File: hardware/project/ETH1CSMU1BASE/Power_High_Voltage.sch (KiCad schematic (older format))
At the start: 124 parts

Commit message: Power supply design
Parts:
- removed C?: 1u/50V, symbol Device:C
- removed C? (x3): 4p7, symbol Device:C
- removed C? (x7): 1u, symbol Device:C
- removed C?: 220n, Capacitor_SMD:C_0603_1608Metric_Pad1.05x0.95mm_HandSolder, symbol Device:C
- removed C? (x2): 10u/100V, symbol Device:C
- removed C? (x3): 1u/250V, symbol Device:C
- removed C?: 100n, symbol Device:C
- removed C? (x6): 4u7/50V, symbol Device:C
- removed C? (x4): 2u2/50V, symbol Device:C
- removed D? (x3): RGF1G-E3/67A, symbol Device:D
- removed D? (x2): PMEG6010CEJ, symbol Device:D
- removed FB? (x2): Ferrite_Bead, symbol Device:Ferrite_Bead
- removed FB? (x2): 742792040, symbol Device:Ferrite_Bead
- removed L?: 330u, symbol Device:L
- removed L?: 100u, symbol Device:L
- removed L? (x4): 74489440068, symbol ETH1CSMU1:74489440068
- removed R? (x8): 1M, symbol Device:R
- removed R?: 215k, symbol Device:R
- removed R?: 10, symbol Device:R
- removed R? (x4): R, symbol Device:R
- removed R? (x2): 154k, symbol Device:R
- removed R? (x3): 287k, symbol Device:R
- removed U? (x2): LT8331EMSE#PBF, ETH1CSMU1:MSE-16, symbol ETH1CSMU1:LT8331
- removed U? (x2): LT8330_S6, symbol ETH1CSMU1:LT8330_S6
- removed U?: MC7815ABD2TR4G, symbol Regulator_Linear:L7815
- removed U?: MC7915BD2TG, symbol Regulator_Linear:L7915
- added C804, C837, C838, C864: 10u/50V, symbol Device:C
- added C805: 4u7/100V, symbol Device:C
- added C808, C824, C828, C832, C844, C861, C862, C863: 4u7/50V, symbol Device:C
- added C809, C815, C848, C851: 1u, symbol Device:C
- added C810: 10n, symbol Device:C
- added C816, C845, C855: 1u/HC, symbol Device:C
- added C819, C820, C852, C860: 4p7, symbol Device:C
- added C821, C825, C856, C858: 1u/400V, symbol Device:C
- added C829: 10u/100V, symbol Device:C
- added C841: 220n, symbol Device:C
- added D801: RB558VA150TR, symbol Device:D_Schottky
- added D802, D807: PMEG6010EP,115, symbol Device:D_Schottky
- added D803, D806: BAV21W, symbol Device:D_Schottky
- added L706, L709, L713, L716: 74489440068, symbol ETH1CSMU1:74489440068
- added L803: 744066101, symbol Device:L
- added L804: CDRH8D43RT125NP-331, symbol Device:L
- added R801, R803, R806, R808, R810, R823, R826, R828: 1M, symbol Device:R
- added R802, R821: 215k, symbol Device:R
- added R804, R824: 287k, symbol Device:R
- added R805: 63k4, symbol Device:R
- added R807: 13k3, symbol Device:R
- added R809: 97k6, symbol Device:R
- added R822: 154k, symbol Device:R
- added R825: 10/2W, symbol Device:R
- added R827: 6k7, symbol Device:R
- added R829: 46k4, symbol Device:R
- added U801, U808: LT8331, symbol ETH1CSMU1:LT8331
- added U802, U809: LT8330_S6, symbol ETH1CSMU1:LT8330_S6
- added U805: MC7815BD2TG, symbol Regulator_Linear:L7815
- added U810: MC7915BD2TG, Package_TO_SOT_SMD:TO-252-2, symbol Regulator_Linear:MC79M15_TO252
- C843, C847, C854, C859: renamed from C?; value 100n/100V -> 100n/200V
- C850: renamed from C?; value 10u/50V -> 10u/200V
- gave numbers to parts that had none: 51
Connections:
- net labels added: GNDF, GNDO
- net labels removed: GNDHV
- wire segments 448 -> 454
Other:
- note removed: "744066100"
- note removed: "CDRH8D43RT125NP‐331MC"
- moved on the sheet: C802, C803, C806, C807, C811, C812, C813, C814, C817, C818, C822, C823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

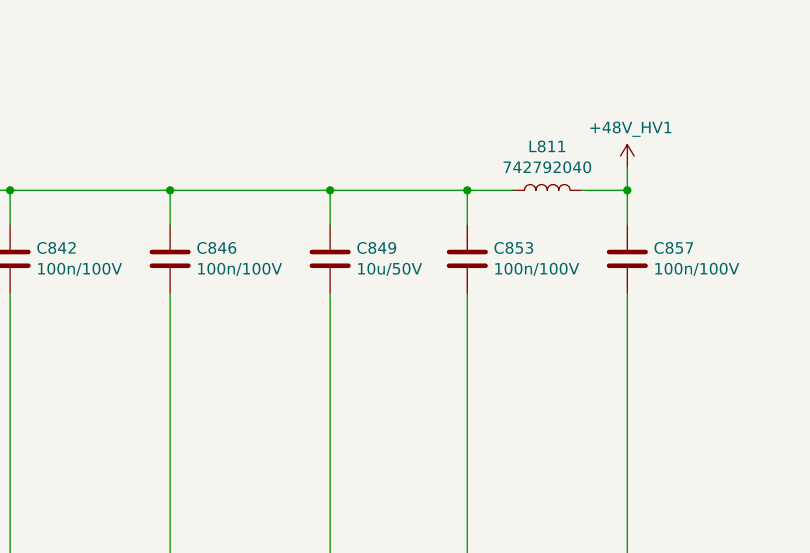
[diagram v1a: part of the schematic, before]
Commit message: Footprint assigment
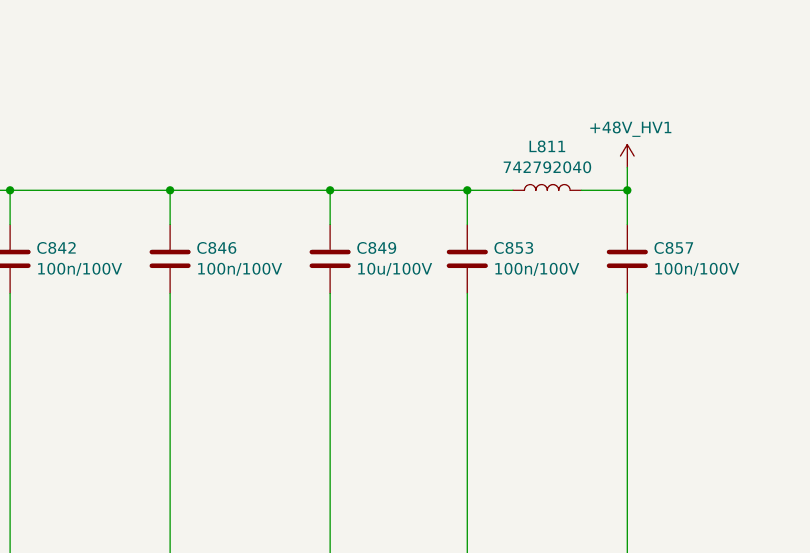
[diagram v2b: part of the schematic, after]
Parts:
- C802, C803, C804, C806, C807, C808, C817, C818, C824, C826, C827, C828, C832, C837, C838, C844, C861, C862, C863, C864: footprint (none) -> Capacitor_SMD:C_1206_3216Metric_Pad1.42x1.75mm_HandSolder
- C809, C810, C815, C819, C820, C830, C831, C833, C834, C835, C836, C839, C840, C841, C848, C851, C852, C860: footprint (none) -> Capacitor_SMD:C_0603_1608Metric_Pad1.05x0.95mm_HandSolder
- C829: footprint (none) -> Capacitor_SMD:C_2220_5650Metric_Pad1.97x5.40mm_HandSolder
- C849: value 10u/50V -> 10u/100V; footprint (none) -> Capacitor_SMD:C_1206_3216Metric_Pad1.42x1.75mm_HandSolder
- D802, D807: footprint (none) -> Diode_SMD:D_SOD-128
- D803, D806: footprint (none) -> Diode_SMD:D_SOD-123F
- L706, L709, L713, L716: footprint (none) -> ETH1CSMU1:74489440068
- R801, R802, R803, R804, R805, R808, R809, R810, R811, R812, R813, R814, R815, R816, R817, R818, R819, R820, R821, R822, R823, R824, R828, R829: footprint (none) -> Resistor_SMD:R_0603_1608Metric_Pad1.05x0.95mm_HandSolder
- U801, U806, U807, U808: footprint (none) -> Package_SO:MSOP-12-16-1EP_3x4mm_P0.5mm_EP1.65x2.85mm
- U802, U809: footprint (none) -> Package_TO_SOT_SMD:TSOT-23-6_HandSoldering
- U805: footprint (none) -> Package_TO_SOT_SMD:TO-263-2
- U810: footprint Package_TO_SOT_SMD:TO-252-2 -> Package_TO_SOT_SMD:TO-263-2

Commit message: Footprint assignment
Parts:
- C604: renamed from C805; footprint (none) -> Capacitor_SMD:C_1210_3225Metric_Pad1.42x2.65mm_HandSolder
- C610: renamed from C811; footprint (none) -> Capacitor_SMD:C_1210_3225Metric_Pad1.42x2.65mm_HandSolder
- C611: renamed from C812; footprint (none) -> Capacitor_SMD:C_1210_3225Metric_Pad1.42x2.65mm_HandSolder
- C612: renamed from C813; footprint (none) -> Capacitor_SMD:C_1210_3225Metric_Pad1.42x2.65mm_HandSolder
- C613: renamed from C814; footprint (none) -> Capacitor_SMD:C_1210_3225Metric_Pad1.42x2.65mm_HandSolder
- C615: renamed from C816; footprint (none) -> Capacitor_SMD:C_1206_3216Metric_Pad1.42x1.75mm_HandSolder
- C618: renamed from C822; footprint (none) -> Capacitor_SMD:C_2220_5650Metric_Pad1.97x5.40mm_HandSolder
- C619: renamed from C823; footprint (none) -> Capacitor_SMD:C_2220_5650Metric_Pad1.97x5.40mm_HandSolder
- C624: renamed from C821; footprint (none) -> Capacitor_SMD:C_2220_5650Metric_Pad1.97x5.40mm_HandSolder
- C626: renamed from C825; footprint (none) -> Capacitor_SMD:C_2220_5650Metric_Pad1.97x5.40mm_HandSolder
- C642: renamed from C845; footprint (none) -> Capacitor_SMD:C_1206_3216Metric_Pad1.42x1.75mm_HandSolder
- C644: renamed from C842; footprint (none) -> Capacitor_SMD:C_1206_3216Metric_Pad1.42x1.75mm_HandSolder
- C645: renamed from C843; value 100n/200V -> 100n/100V; footprint (none) -> Capacitor_SMD:C_1206_3216Metric_Pad1.42x1.75mm_HandSolder
- C646: renamed from C846; footprint (none) -> Capacitor_SMD:C_1206_3216Metric_Pad1.42x1.75mm_HandSolder
- C647: renamed from C847; value 100n/200V -> 100n/100V; footprint (none) -> Capacitor_SMD:C_1206_3216Metric_Pad1.42x1.75mm_HandSolder
- C649: renamed from C849; footprint Capacitor_SMD:C_1206_3216Metric_Pad1.42x1.75mm_HandSolder -> Capacitor_SMD:C_2220_5650Metric_Pad1.97x5.40mm_HandSolder
- C650: renamed from C850; value 10u/200V -> 10u/100V; footprint (none) -> Capacitor_SMD:C_2220_5650Metric_Pad1.97x5.40mm_HandSolder
- C652: renamed from C855; footprint (none) -> Capacitor_SMD:C_1206_3216Metric_Pad1.42x1.75mm_HandSolder
- C653: renamed from C856; footprint (none) -> Capacitor_SMD:C_2220_5650Metric_Pad1.97x5.40mm_HandSolder
- C654: renamed from C853; footprint (none) -> Capacitor_SMD:C_1206_3216Metric_Pad1.42x1.75mm_HandSolder
- C655: renamed from C854; value 100n/200V -> 100n/100V; footprint (none) -> Capacitor_SMD:C_1206_3216Metric_Pad1.42x1.75mm_HandSolder
- C656: renamed from C858; footprint (none) -> Capacitor_SMD:C_2220_5650Metric_Pad1.97x5.40mm_HandSolder
- C657: renamed from C857; footprint (none) -> Capacitor_SMD:C_1206_3216Metric_Pad1.42x1.75mm_HandSolder
- C658: renamed from C859; value 100n/200V -> 100n/100V; footprint (none) -> Capacitor_SMD:C_1206_3216Metric_Pad1.42x1.75mm_HandSolder
- D601: renamed from D801; value RB558VA150TR -> RB558VAM150; footprint (none) -> ETH1CSMU1:D_SOD-323HE
- D602: renamed from D802; footprint Diode_SMD:D_SOD-128 -> ETH1CSMU1:D_SOD-128
- D603: renamed from D804; footprint (none) -> ETH1CSMU1:PowerDI-123
- D604: renamed from D805; footprint (none) -> ETH1CSMU1:PowerDI-123
- D607: renamed from D807; footprint Diode_SMD:D_SOD-128 -> ETH1CSMU1:D_SOD-128
- L603: renamed from L803; footprint (none) -> ETH1CSMU1:744066101
- L604: renamed from L806; footprint (none) -> Inductor_SMD:L_0805_2012Metric_Pad1.15x1.40mm_HandSolder
- L605: renamed from L805; footprint (none) -> Inductor_SMD:L_0805_2012Metric_Pad1.15x1.40mm_HandSolder
- L606: renamed from L807; footprint (none) -> ETH1CSMU1:74437324068
- L607: renamed from L808; footprint (none) -> ETH1CSMU1:74437324068
- L609: renamed from L811; footprint (none) -> Inductor_SMD:L_0805_2012Metric_Pad1.15x1.40mm_HandSolder
- L610: renamed from L812; footprint (none) -> Inductor_SMD:L_0805_2012Metric_Pad1.15x1.40mm_HandSolder
- R606: renamed from R806; footprint (none) -> Resistor_SMD:R_0805_2012Metric_Pad1.15x1.40mm_HandSolder
- R607: renamed from R807; footprint (none) -> Resistor_SMD:R_0805_2012Metric_Pad1.15x1.40mm_HandSolder
- R625: renamed from R825; value 10/2W -> 10/1W; footprint (none) -> Resistor_SMD:R_2512_6332Metric_Pad1.52x3.35mm_HandSolder
- R626: renamed from R826; footprint (none) -> Resistor_SMD:R_0805_2012Metric_Pad1.15x1.40mm_HandSolder
- R627: renamed from R827; footprint (none) -> Resistor_SMD:R_0805_2012Metric_Pad1.15x1.40mm_HandSolder
- U603: renamed from U803; footprint (none) -> ETH1CSMU1:TEL10
- U604: renamed from U804; footprint (none) -> ETH1CSMU1:TEL10
- renumbered C802 to C601, C803 to C602, C804 to C603, C806 to C605, C807 to C606, C808 to C607, C809 to C608, C810 to C609, C815 to C614, C817 to C616, C818 to C617, C819 to C620, C820 to C621, C826 to C622, C827 to C623, C824 to C625, C828 to C627, C830 to C628, C831 to C629, C829 to C630, C832 to C631, C833 to C632, C834 to C633, C835 to C634, C836 to C635, C837 to C636, C838 to C637, C839 to C638, C840 to C639, C841 to C640, C844 to C641, C848 to C643, C851 to C648, C852 to C651, C860 to C659, C861 to C660, C862 to C661, C863 to C662, C864 to C663, D803 to D605, D806 to D606, L709 to L504, L706 to L506, L716 to L508, L713 to L509, L801 to L601, L802 to L602, L804 to L608, R801 to R601, R802 to R602, R803 to R603, R804 to R604, R805 to R605, R808 to R608, R809 to R609, R811 to R610, R812 to R611, R813 to R612, R814 to R613, R815 to R614, R816 to R615, R810 to R616, R821 to R617, R817 to R618, R818 to R619, R819 to R620, R820 to R621, R822 to R622, R823 to R623, R824 to R624, R828 to R628, R829 to R629, U801 to U601, U802 to U602, U806 to U605, U807 to U606, U805 to U607, U808 to U608, U809 to U609, U810 to U610
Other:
- moved on the sheet: L605
